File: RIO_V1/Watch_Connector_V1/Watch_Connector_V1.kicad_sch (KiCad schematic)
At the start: 2 parts, among them J1 Conn_01x04_Socket, J2 Conn_01x04_Pin

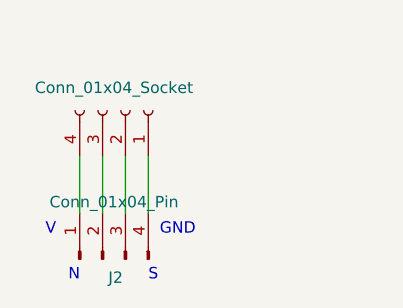
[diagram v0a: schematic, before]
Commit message: Changed The FPC Connector To A Smaller Pitch
Changed the FPC connector on the PCB so that the pitch is reduced and overall footprint is minimized as much as possible
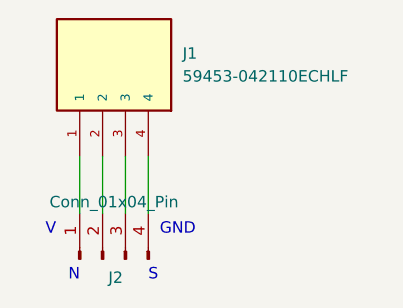
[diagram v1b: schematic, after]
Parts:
- removed J1: Conn_01x04_Socket, Connector_FFC-FPC:TE_84952-4_1x04-1MP_P1.0mm_Horizontal, symbol Connector:Conn_01x04_Socket
- added J1: 59453-042110ECHLF, Connector:AMPHENOL_59453-042110ECHLF, symbol Connector:59453-042110ECHLF
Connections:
- net at J2.1 (Pin_1): now also J1.1
- net at J2.2 (Pin_2): now also J1.2
- net at J2.3 (Pin_3): now also J1.3
- net at J2.4 (Pin_4): now also J1.4
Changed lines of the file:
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@@
     )
   )
-  (symbol (lib_id "Connector:Conn_01x04_Socket") (at 127 64.77 270) (mirror x) (unit 1)
-    (in_bom yes) (on_board yes) (dnp no)
-    (property "Reference" "J1" (at 125.73 71.12 90)
+  (symbol (lib_id "Connector:59453-042110ECHLF") (at 124.46 59.69 90) (unit 1)
+    (in_bom yes) (on_board yes) (dnp no) (fields_autoplaced)
+    (property "Reference" "J1" (at 133.35 58.42 90)
+      (effects (font (size 1.27 1.27)) (justify right))
+    )
+    (property "Value" "59453-042110ECHLF" (at 133.35 60.96 90)
+      (effects (font (size 1.27 1.27)) (justify right))
+    )
+    (property "Footprint" "Connector:AMPHENOL_59453-042110ECHLF" (at 124.46 59.69 0)
+      (effects (font (size 1.27 1.27)) (justify bottom) hide)
+    )
+    (property "Datasheet" "" (at 124.46 59.69 0)
       (effects (font (size 1.27 1.27)) hide)
     )
-    (property "Value" "Conn_01x04_Socket" (at 125.73 62.23 90)
-      (effects (font (size 1.27 1.27)))
+    (property "DigiKey_Part_Number" "609-59453-042110ECHLFTR-ND" (at 124.46 59.69 0)
+      (effects (font (size 1.27 1.27)) (justify bottom) hide)
     )
-    (property "Footprint" "Connector_FFC-FPC:TE_84952-4_1x04-1MP_P1.0mm_Horizontal" (at 127 64.77 0)
-      (effects (font (size 1.27 1.27)) hide)
+    (property "SnapEDA_Link" "https://www.snapeda.com/parts/59453-042110ECHLF/Amphenol/view-part/?ref=snap" (at 124.46 59.69 0)
+      (effects (font (size 1.27 1.27)) (justify bottom) hide)
     )
-    (property "Datasheet" "~" (at 127 64.77 0)
-      (effects (font (size 1.27 1.27)) hide)
+    (property "MAXIMUM_PACKAGE_HEIGHT" "3mm" (at 124.46 59.69 0)
+      (effects (font (size 1.27 1.27)) (justify bottom) hide)
+    )
+    (property "Package" "None" (at 124.46 59.69 0)
+      (effects (font (size 1.27 1.27)) (justify bottom) hide)
+    )
+    (property "Check_prices" "https://www.snapeda.com/parts/59453-042110ECHLF/Amphenol/view-part/?ref=eda" (at 124.46 59.69 0)
+      (effects (font (size 1.27 1.27)) (justify bottom) hide)
+    )
+    (property "STANDARD" "Manufacturer Recommendations" (at 124.46 59.69 0)
+      (effects (font (size 1.27 1.27)) (justify bottom) hide)
+    )
+    (property "PARTREV" "A" (at 124.46 59.69 0)
+      (effects (font (size 1.27 1.27)) (justify bottom) hide)
+    )
+    (property "MF" "AMPHENOL ICC / FCI" (at 124.46 59.69 0)
+      (effects (font (size 1.27 1.27)) (justify bottom) hide)
+    )
+    (property "MP" "59453-042110ECHLF" (at 124.46 59.69 0)
+      (effects (font (size 1.27 1.27)) (justify bottom) hide)
+    )
+    (property "Description" "\n0.50mm Flex Connectors, FPC/FFC Side Entry ZIF Connector, Surface Mount, 4 Positions, Top Contact, 0.50mm (0.020in) Pitch.\n" (at 124.46 59.69 0)
+      (effects (font (size 1.27 1.27)) (justify bottom) hide)
+    )
+    (property "MANUFACTURER" "Amphenol" (at 124.46 59.69 0)
+      (effects (font (size 1.27 1.27)) (justify bottom) hide)
+    )
+    (property "SNAPEDA_PN" "59453-042110ECHLF" (at 124.46 59.69 0)
+      (effects (font (size 1.27 1.27)) (justify bottom) hide)
     )
     (pin "3")
+    (pin "1")
     (pin "4")
-    (pin "1")
     (pin "2")
     (instances
